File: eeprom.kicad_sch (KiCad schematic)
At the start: 5 parts, among them U701 24LC32

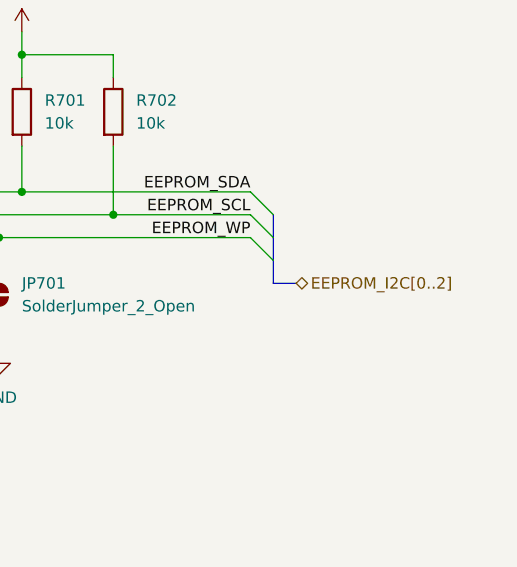
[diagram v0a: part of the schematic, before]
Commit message: added net-classes
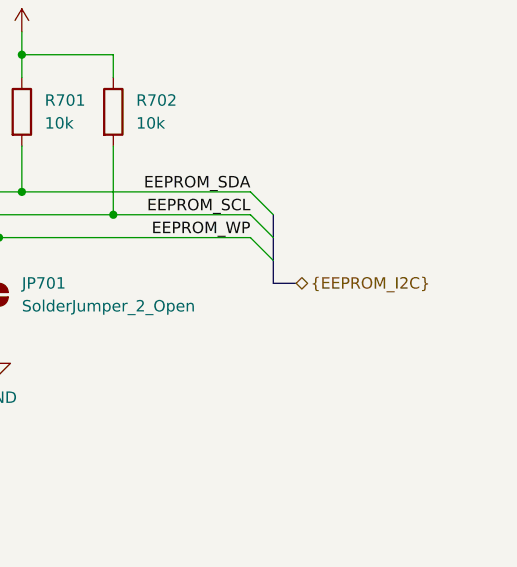
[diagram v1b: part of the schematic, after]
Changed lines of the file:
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@@
     (effects (font (size 1.27 1.27)) (justify right bottom))
   )
-  (hierarchical_label "EEPROM_I2C[0..2]" (shape bidirectional) (at 160.02 64.77 0) (fields_autoplaced)
+  (hierarchical_label "{EEPROM_I2C}" (shape bidirectional) (at 160.02 64.77 0) (fields_autoplaced)
     (effects (font (size 1.27 1.27)) (justify left))
   )

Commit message: completed schematic
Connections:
- net +3V3 renamed +3.3V

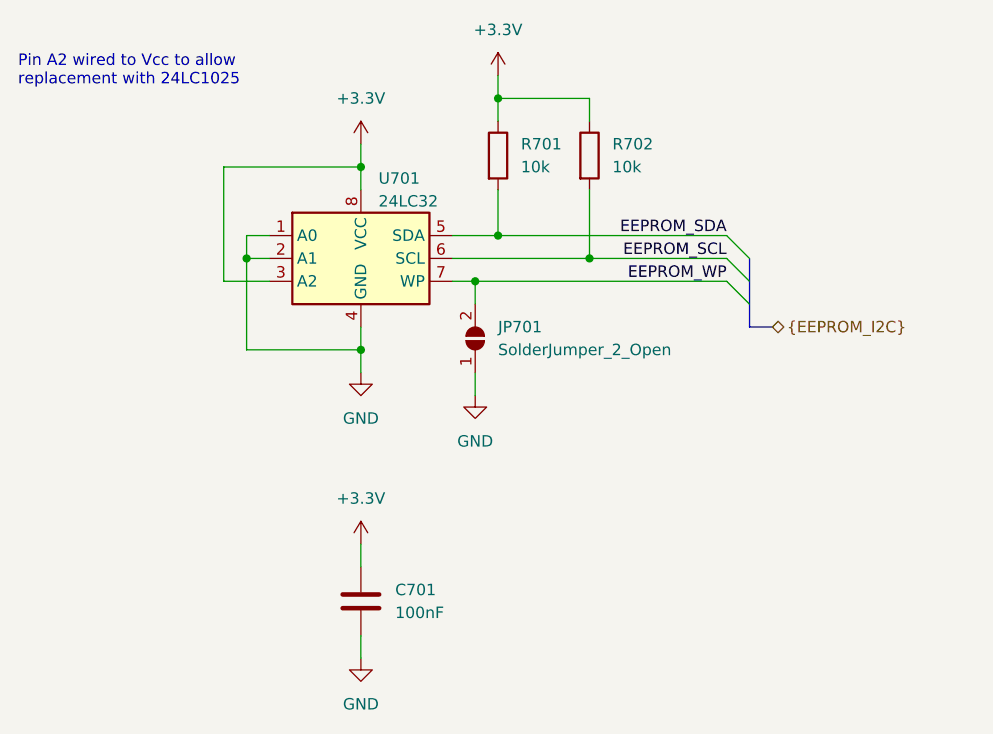
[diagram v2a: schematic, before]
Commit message: hierarchical sheets for digital I/O and replaced power supply jumpers with relays
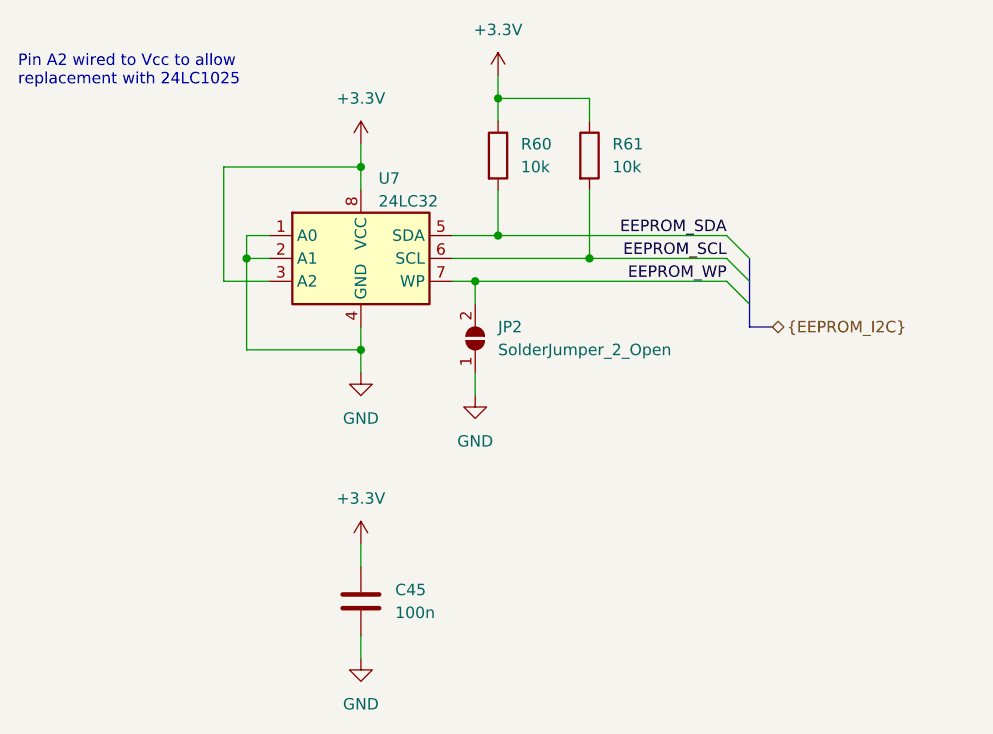
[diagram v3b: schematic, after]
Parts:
- C45: renamed from C701; value 100nF -> 100n
- renumbered JP701 to JP2, R701 to R60, R702 to R61, U701 to U7
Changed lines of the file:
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@@
   (symbol (lib_id "power:+3.3V") (at 114.3 44.45 0) (unit 1)
     (in_bom yes) (on_board yes) (dnp no) (fields_autoplaced)
-    (property "Reference" "#PWR0702" (at 114.3 48.26 0)
+    (property "Reference" "#PWR0106" (at 114.3 48.26 0)
       (effects (font (size 1.27 1.27)) hide)
     )
@@
       (project "Sensor_Board"
         (path "/e2a0eb17-0eae-4cdd-befd-118f8728b921/e07e8d3e-2464-4609-a06b-1a513999ec7c"
-          (reference "#PWR0702") (unit 1)
+          (reference "#PWR0106") (unit 1)
         )
       )
@@
   (symbol (lib_id "power:GND") (at 114.3 69.85 0) (unit 1)
     (in_bom yes) (on_board yes) (dnp no) (fields_autoplaced)
-    (property "Reference" "#PWR0703" (at 114.3 76.2 0)
+    (property "Reference" "#PWR0107" (at 114.3 76.2 0)
       (effects (font (size 1.27 1.27)) hide)
     )
@@
       (project "Sensor_Board"
         (path "/e2a0eb17-0eae-4cdd-befd-118f8728b921/e07e8d3e-2464-4609-a06b-1a513999ec7c"
-          (reference "#PWR0703") (unit 1)
+          (reference "#PWR0107") (unit 1)
         )
       )
@@
   (symbol (lib_id "Device:R") (at 129.54 45.72 0) (unit 1)
     (in_bom yes) (on_board yes) (dnp no) (fields_autoplaced)
-    (property "Reference" "R701" (at 132.08 44.4499 0)
+    (property "Reference" "R60" (at 132.08 44.4499 0)
       (effects (font (size 1.27 1.27)) (justify left))
     )
@@
       (project "Sensor_Board"
         (path "/e2a0eb17-0eae-4cdd-befd-118f8728b921/e07e8d3e-2464-4609-a06b-1a513999ec7c"
-          (reference "R701") (unit 1)
+          (reference "R60") (unit 1)
         )
       )
@@
   (symbol (lib_id "Jumper:SolderJumper_2_Open") (at 127 66.04 90) (unit 1)
     (in_bom yes) (on_board yes) (dnp no) (fields_autoplaced)
-    (property "Reference" "JP701" (at 129.54 64.7699 90)
+    (property "Reference" "JP2" (at 129.54 64.7699 90)
       (effects (font (size 1.27 1.27)) (justify right))
     )
@@
       (project "Sensor_Board"
         (path "/e2a0eb17-0eae-4cdd-befd-118f8728b921/e07e8d3e-2464-4609-a06b-1a513999ec7c"
-          (reference "JP701") (unit 1)
+          (reference "JP2") (unit 1)
         )
       )
@@
   (symbol (lib_id "Device:C") (at 114.3 95.25 0) (unit 1)
     (in_bom yes) (on_board yes) (dnp no) (fields_autoplaced)
-    (property "Reference" "C701" (at 118.11 93.9799 0)
-      (effects (font (size 1.27 1.27)) (justify left))
-    )
-    (property "Value" "100nF" (at 118.11 96.5199 0)
+    (property "Reference" "C45" (at 118.11 93.9799 0)
+      (effects (font (size 1.27 1.27)) (justify left))
+    )
+    (property "Value" "100n" (at 118.11 96.5199 0)
       (effects (font (size 1.27 1.27)) (justify left))
     )
@@
       (project "Sensor_Board"
         (path "/e2a0eb17-0eae-4cdd-befd-118f8728b921/e07e8d3e-2464-4609-a06b-1a513999ec7c"
-          (reference "C701") (unit 1)
+          (reference "C45") (unit 1)
         )
       )
@@
   (symbol (lib_id "power:GND") (at 114.3 101.6 0) (unit 1)
     (in_bom yes) (on_board yes) (dnp no) (fields_autoplaced)
-    (property "Reference" "#PWR0706" (at 114.3 107.95 0)
+    (property "Reference" "#PWR0110" (at 114.3 107.95 0)
       (effects (font (size 1.27 1.27)) hide)
     )
@@
       (project "Sensor_Board"
         (path "/e2a0eb17-0eae-4cdd-befd-118f8728b921/e07e8d3e-2464-4609-a06b-1a513999ec7c"
-          (reference "#PWR0706") (unit 1)
+          (reference "#PWR0110") (unit 1)
         )
       )
@@
   (symbol (lib_id "power:+3.3V") (at 129.54 36.83 0) (unit 1)
     (in_bom yes) (on_board yes) (dnp no) (fields_autoplaced)
-    (property "Reference" "#PWR0701" (at 129.54 40.64 0)
+    (property "Reference" "#PWR0105" (at 129.54 40.64 0)
       (effects (font (size 1.27 1.27)) hide)
     )
@@
       (project "Sensor_Board"
         (path "/e2a0eb17-0eae-4cdd-befd-118f8728b921/e07e8d3e-2464-4609-a06b-1a513999ec7c"
-          (reference "#PWR0701") (unit 1)
+          (reference "#PWR0105") (unit 1)
         )
       )
@@
   (symbol (lib_id "Device:R") (at 139.7 45.72 0) (unit 1)
     (in_bom yes) (on_board yes) (dnp no) (fields_autoplaced)
-    (property "Reference" "R702" (at 142.24 44.4499 0)
+    (property "Reference" "R61" (at 142.24 44.4499 0)
       (effects (font (size 1.27 1.27)) (justify left))
     )
@@
       (project "Sensor_Board"
         (path "/e2a0eb17-0eae-4cdd-befd-118f8728b921/e07e8d3e-2464-4609-a06b-1a513999ec7c"
-          (reference "R702") (unit 1)
+          (reference "R61") (unit 1)
         )
       )
@@
   (symbol (lib_id "Memory_EEPROM:24LC32") (at 114.3 57.15 0) (unit 1)
     (in_bom yes) (on_board yes) (dnp no) (fields_autoplaced)
-    (property "Reference" "U701" (at 116.2559 48.26 0)
+    (property "Reference" "U7" (at 116.2559 48.26 0)
       (effects (font (size 1.27 1.27)) (justify left))
     )
@@
       (project "Sensor_Board"
         (path "/e2a0eb17-0eae-4cdd-befd-118f8728b921/e07e8d3e-2464-4609-a06b-1a513999ec7c"
-          (reference "U701") (unit 1)
+          (reference "U7") (unit 1)
         )
       )
@@
   (symbol (lib_id "power:+3.3V") (at 114.3 88.9 0) (unit 1)
     (in_bom yes) (on_board yes) (dnp no) (fields_autoplaced)
-    (property "Reference" "#PWR0705" (at 114.3 92.71 0)
+    (property "Reference" "#PWR0109" (at 114.3 92.71 0)
       (effects (font (size 1.27 1.27)) hide)
     )
@@
       (project "Sensor_Board"
         (path "/e2a0eb17-0eae-4cdd-befd-118f8728b921/e07e8d3e-2464-4609-a06b-1a513999ec7c"
-          (reference "#PWR0705") (unit 1)
+          (reference "#PWR0109") (unit 1)
         )
       )
@@
   (symbol (lib_id "power:GND") (at 127 72.39 0) (unit 1)
     (in_bom yes) (on_board yes) (dnp no) (fields_autoplaced)
-    (property "Reference" "#PWR0704" (at 127 78.74 0)
+    (property "Reference" "#PWR0108" (at 127 78.74 0)
       (effects (font (size 1.27 1.27)) hide)
     )
@@
       (project "Sensor_Board"
         (path "/e2a0eb17-0eae-4cdd-befd-118f8728b921/e07e8d3e-2464-4609-a06b-1a513999ec7c"
-          (reference "#PWR0704") (unit 1)
-        )
-      )
+          (reference "#PWR0108") (unit 1)
+        )
+      )
